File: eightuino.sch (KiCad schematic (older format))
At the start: 23 parts, among them CON1 BARREL_JACK, P1 PowerPins, P3 Digital1, P4 Digital_2, P5 Serial, P6 ISP, SW1 SW_PUSH_SMALL, U1 NCP1117ST33T3G, X1 CRYSTAL

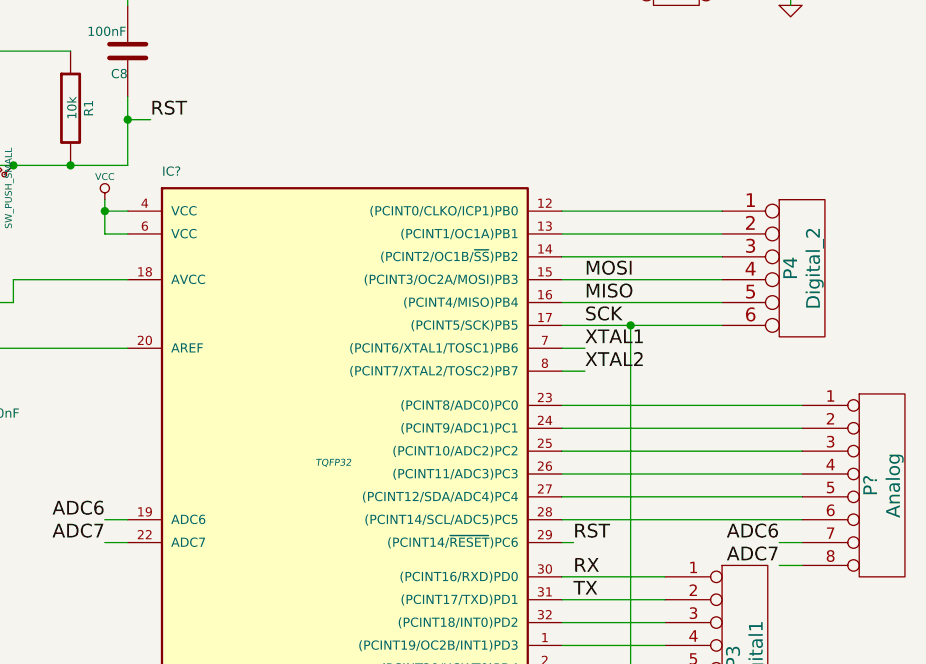
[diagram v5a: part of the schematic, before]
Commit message: Updated netlist and components to SMD
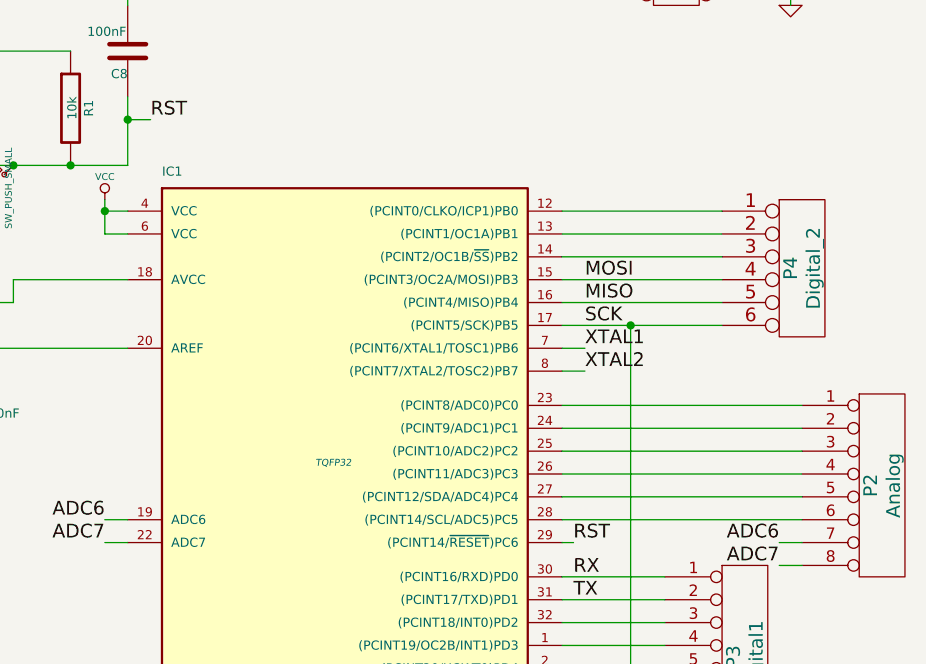
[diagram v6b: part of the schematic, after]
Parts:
- gave numbers to parts that had none: 2
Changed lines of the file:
@@
 $EndComp
 $Comp
-L GND #PWR16
+L GND #PWR01
 U 1 1 528D0B5A
 P 5300 3300
-F 0 "#PWR16" H 5300 3300 30  0001 C CNN
+F 0 "#PWR01" H 5300 3300 30  0001 C CNN
 F 1 "GND" H 5300 3230 30  0001 C CNN
 F 2 "" H 5300 3300 60  0000 C CNN
@@
 $EndComp
 $Comp
-L GND #PWR14
+L GND #PWR02
 U 1 1 528D0B67
 P 5100 3300
-F 0 "#PWR14" H 5100 3300 30  0001 C CNN
+F 0 "#PWR02" H 5100 3300 30  0001 C CNN
 F 1 "GND" H 5100 3230 30  0001 C CNN
 F 2 "" H 5100 3300 60  0000 C CNN
@@
 $EndComp
 $Comp
-L GND #PWR13
+L GND #PWR03
 U 1 1 528D0B6D
 P 4900 3300
-F 0 "#PWR13" H 4900 3300 30  0001 C CNN
+F 0 "#PWR03" H 4900 3300 30  0001 C CNN
 F 1 "GND" H 4900 3230 30  0001 C CNN
 F 2 "" H 4900 3300 60  0000 C CNN
@@
 $EndComp
 $Comp
-L GND #PWR11
+L GND #PWR04
 U 1 1 528D0D22
 P 4700 2650
-F 0 "#PWR11" H 4700 2650 30  0001 C CNN
+F 0 "#PWR04" H 4700 2650 30  0001 C CNN
 F 1 "GND" H 4700 2580 30  0001 C CNN
 F 2 "" H 4700 2650 60  0000 C CNN
@@
 $EndComp
 $Comp
-L GND #PWR15
+L GND #PWR05
 U 1 1 528D1116
 P 5250 2250
-F 0 "#PWR15" H 5250 2250 30  0001 C CNN
+F 0 "#PWR05" H 5250 2250 30  0001 C CNN
 F 1 "GND" H 5250 2180 30  0001 C CNN
 F 2 "" H 5250 2250 60  0000 C CNN
@@
 $EndComp
 $Comp
-L GND #PWR4
+L GND #PWR06
 U 1 1 5293AE0F
 P 2500 6000
-F 0 "#PWR4" H 2500 6000 30  0001 C CNN
+F 0 "#PWR06" H 2500 6000 30  0001 C CNN
 F 1 "GND" H 2500 5930 30  0001 C CNN
 F 2 "" H 2500 6000 60  0000 C CNN
@@
 $EndComp
 $Comp
-L GND #PWR6
+L GND #PWR07
 U 1 1 5293AEC4
 P 3100 6900
-F 0 "#PWR6" H 3100 6900 30  0001 C CNN
+F 0 "#PWR07" H 3100 6900 30  0001 C CNN
 F 1 "GND" H 3100 6830 30  0001 C CNN
 F 2 "" H 3100 6900 60  0000 C CNN
@@
 $EndComp
 $Comp
-L GND #PWR5
+L GND #PWR08
 U 1 1 5293AF43
 P 2600 7050
-F 0 "#PWR5" H 2600 7050 30  0001 C CNN
+F 0 "#PWR08" H 2600 7050 30  0001 C CNN
 F 1 "GND" H 2600 6980 30  0001 C CNN
 F 2 "" H 2600 7050 60  0000 C CNN
@@
 $EndComp
 $Comp
-L GND #PWR8
+L GND #PWR09
 U 1 1 5293AF49
 P 3600 7050
-F 0 "#PWR8" H 3600 7050 30  0001 C CNN
+F 0 "#PWR09" H 3600 7050 30  0001 C CNN
 F 1 "GND" H 3600 6980 30  0001 C CNN
 F 2 "" H 3600 7050 60  0000 C CNN
@@
 $EndComp
 $Comp
-L GND #PWR3
+L GND #PWR010
 U 1 1 52B96E7A
 P 2100 1750
-F 0 "#PWR3" H 2100 1750 30  0001 C CNN
+F 0 "#PWR010" H 2100 1750 30  0001 C CNN
 F 1 "GND" H 2100 1680 30  0001 C CNN
 F 2 "" H 2100 1750 60  0000 C CNN
@@
 $EndComp
 $Comp
-L +BATT #PWR2
+L +BATT #PWR011
 U 1 1 52B97066
 P 2100 900
-F 0 "#PWR2" H 2100 850 20  0001 C CNN
+F 0 "#PWR011" H 2100 850 20  0001 C CNN
 F 1 "+BATT" H 2100 1000 30  0000 C CNN
 F 2 "" H 2100 900 60  0000 C CNN
@@
 $EndComp
 $Comp
-L +BATT #PWR12
+L +BATT #PWR012
 U 1 1 52B9707A
 P 4900 1600
-F 0 "#PWR12" H 4900 1550 20  0001 C CNN
+F 0 "#PWR012" H 4900 1550 20  0001 C CNN
 F 1 "+BATT" H 4900 1700 30  0000 C CNN
 F 2 "" H 4900 1600 60  0000 C CNN
@@
 $EndComp
 $Comp
-L GND #PWR1
+L GND #PWR013
 U 1 1 52B97A43
 P 2000 3300
-F 0 "#PWR1" H 2000 3300 30  0001 C CNN
+F 0 "#PWR013" H 2000 3300 30  0001 C CNN
 F 1 "GND" H 2000 3230 30  0001 C CNN
 F 2 "" H 2000 3300 60  0000 C CNN
@@
 $EndComp
 $Comp
-L GND #PWR10
+L GND #PWR014
 U 1 1 52D5A868
 P 4550 3950
-F 0 "#PWR10" H 4550 3950 30  0001 C CNN
+F 0 "#PWR014" H 4550 3950 30  0001 C CNN
 F 1 "GND" H 4550 3880 30  0001 C CNN
 F 2 "" H 4550 3950 60  0000 C CNN
@@
 $EndComp
 $Comp
-L VCC #PWR7
+L VCC #PWR015
 U 1 1 52D5AB5A
 P 3600 6250
-F 0 "#PWR7" H 3600 6350 30  0001 C CNN
+F 0 "#PWR015" H 3600 6350 30  0001 C CNN
 F 1 "VCC" H 3600 6350 30  0000 C CNN
 F 2 "" H 3600 6250 60  0000 C CNN
@@
 $EndComp
 $Comp
-L VCC #PWR9
+L VCC #PWR016
 U 1 1 52D5ACF4
 P 4200 3750
-F 0 "#PWR9" H 4200 3850 30  0001 C CNN
+F 0 "#PWR016" H 4200 3850 30  0001 C CNN
 F 1 "VCC" H 4200 3850 30  0000 C CNN
 F 2 "" H 4200 3750 60  0000 C CNN
@@
 MOSI
 $Comp
-L VCC #PWR18
+L VCC #PWR017
 U 1 1 52D6FB73
 P 8850 950
-F 0 "#PWR18" H 8850 1050 30  0001 C CNN
+F 0 "#PWR017" H 8850 1050 30  0001 C CNN
 F 1 "VCC" H 8850 1050 30  0000 C CNN
 F 2 "" H 8850 950 60  0000 C CNN
@@
 $EndComp
 $Comp
-L GND #PWR19
+L GND #PWR018
 U 1 1 52D6FC04
 P 8850 1300
-F 0 "#PWR19" H 8850 1300 30  0001 C CNN
+F 0 "#PWR018" H 8850 1300 30  0001 C CNN
 F 1 "GND" H 8850 1230 30  0001 C CNN
 F 2 "" H 8850 1300 60  0000 C CNN
@@
 RST
 $Comp
-L GND #PWR17
+L GND #PWR019
 U 1 1 52D7024C
 P 6850 5000
-F 0 "#PWR17" H 6850 5000 30  0001 C CNN
+F 0 "#PWR019" H 6850 5000 30  0001 C CNN
 F 1 "GND" H 6850 4930 30  0001 C CNN
 F 2 "" H 6850 5000 60  0000 C CNN
@@
 	5300 2500 4600 2500
 $Comp
-L ATMEGA328P-A IC?
+L ATMEGA328P-A IC1
 U 1 1 52E2E72B
 P 6850 3300
-F 0 "IC?" H 6100 4550 40  0000 L BNN
+F 0 "IC1" H 6100 4550 40  0000 L BNN
 F 1 "ATMEGA328P-A" H 7250 1900 40  0000 L BNN
 F 2 "TQFP32" H 6850 3300 30  0000 C CIN
@@
 	5200 1700 5200 1500
 $Comp
-L VCC #PWR?
+L VCC #PWR020
 U 1 1 52E2F21D
 P 5850 2150
-F 0 "#PWR?" H 5850 2250 30  0001 C CNN
+F 0 "#PWR020" H 5850 2250 30  0001 C CNN
 F 1 "VCC" H 5850 2250 30  0000 C CNN
 F 2 "" H 5850 2150 60  0000 C CNN
@@
 Connection ~ 5850 2200
 $Comp
-L CONN_8 P?
+L CONN_8 P2
 U 1 1 52E2F32E
 P 9250 3400
-F 0 "P?" V 9200 3400 60  0000 C CNN
+F 0 "P2" V 9200 3400 60  0000 C CNN
 F 1 "Analog" V 9300 3400 60  0000 C CNN
 F 2 "" H 9250 3400 60  0000 C CNN

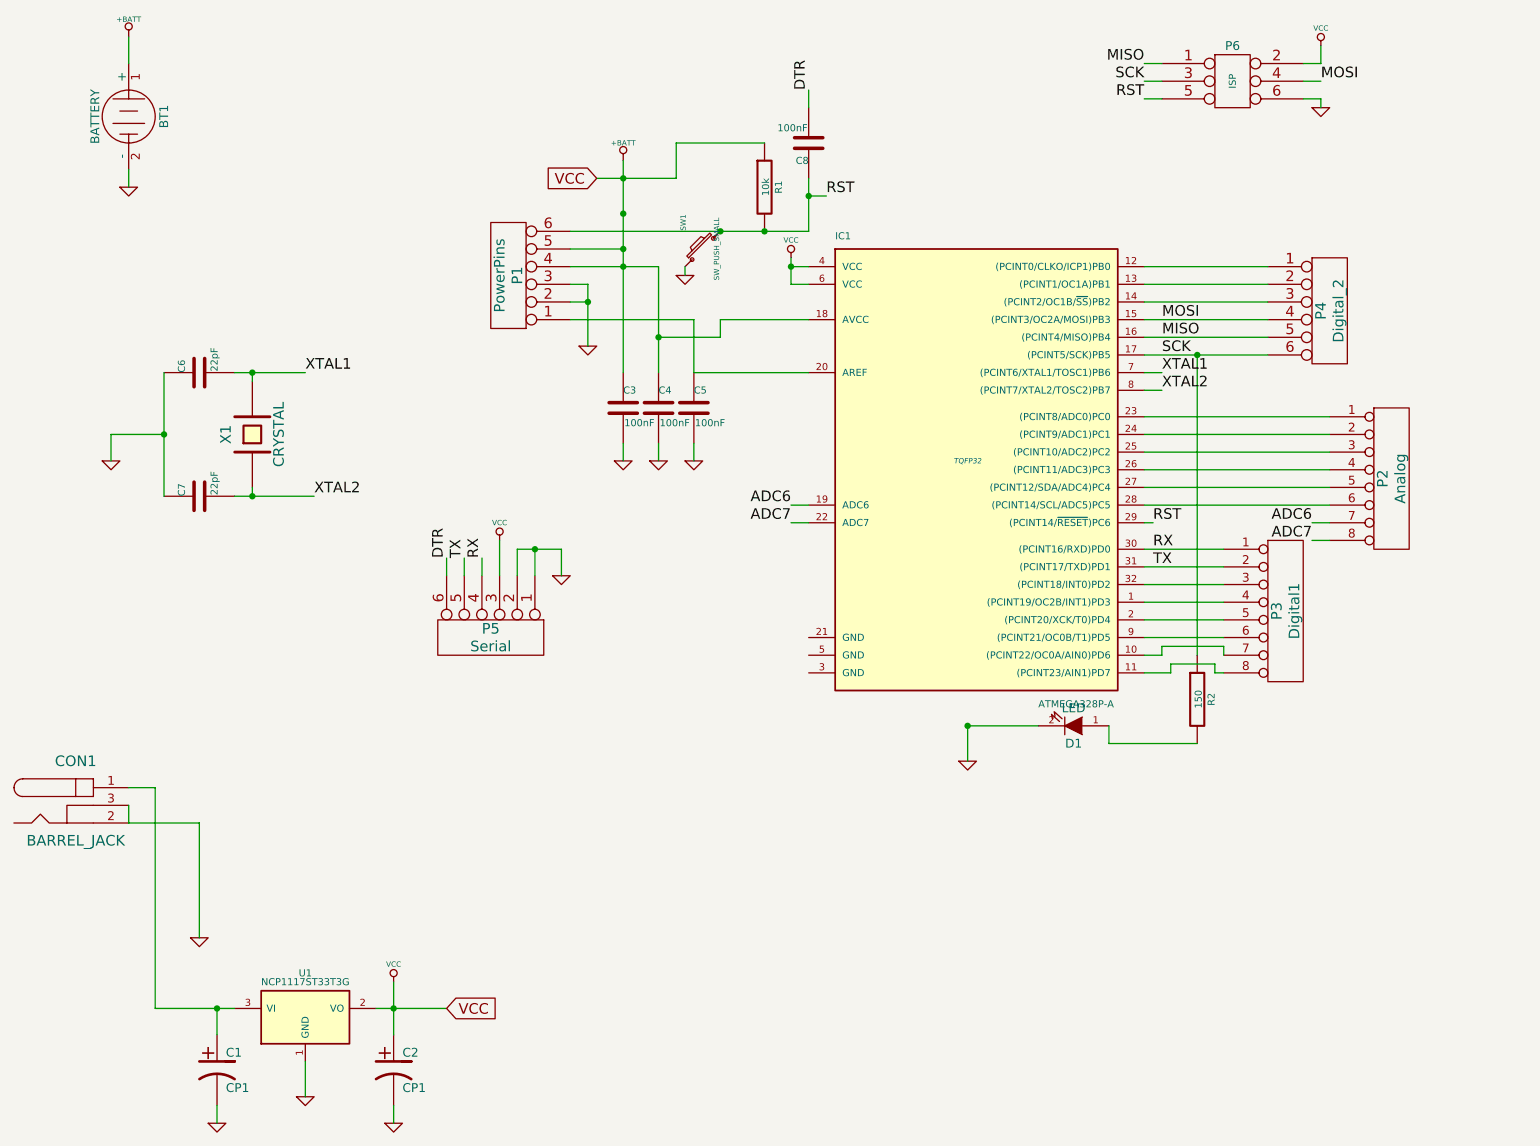
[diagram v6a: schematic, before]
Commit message: Added LC filter at AVCC, cleaned schematic up a bit
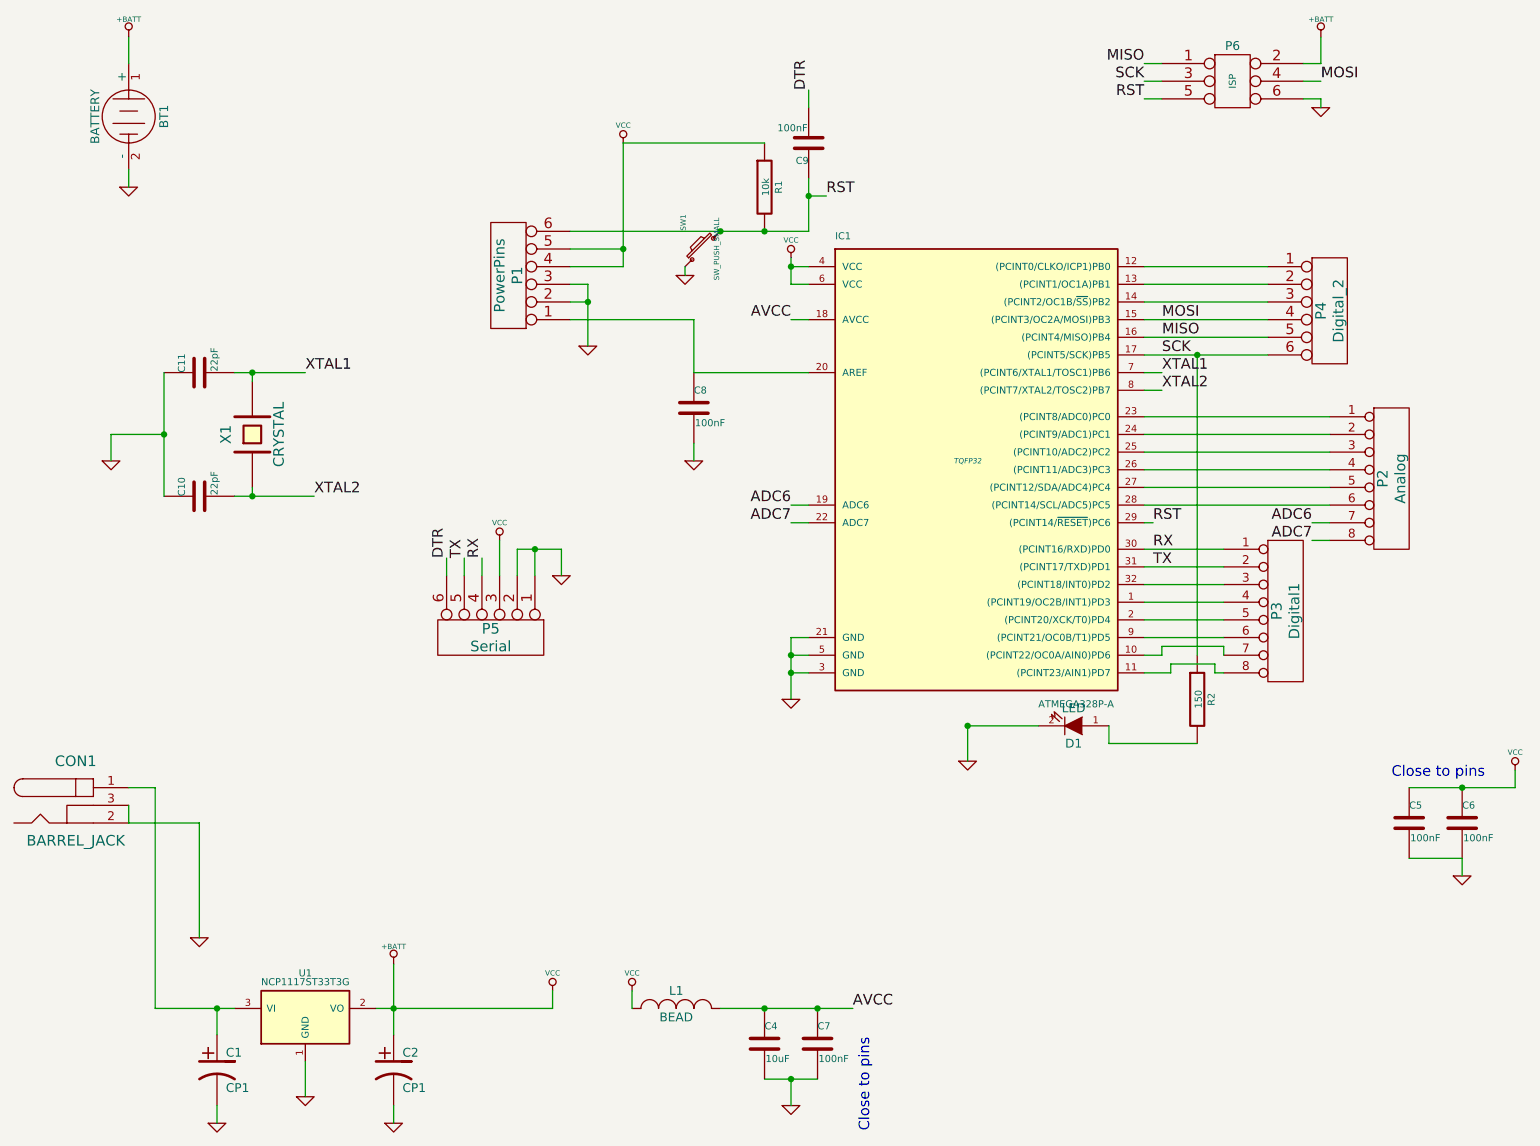
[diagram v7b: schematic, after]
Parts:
- added C4: 10uF, symbol C
- added C5: 100nF, ~, symbol C
- added L1: BEAD, symbol INDUCTOR_SMALL
- renumbered C7 to C10, C6 to C11, C3 to C6, C4 to C7, C5 to C8, C8 to C9
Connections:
- net +BATT: now also C5.1, L1.1; no longer C7.1, IC1.18 (AVCC)
- net GND: now also IC1.21 (GND), IC1.3 (GND), IC1.5 (GND), C4.2, C5.2
- new net AVCC: C4.1, C7.1, IC1.18 (AVCC), L1.2
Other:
- note added: "Close to pins"
- moved on the sheet: C6, C7
